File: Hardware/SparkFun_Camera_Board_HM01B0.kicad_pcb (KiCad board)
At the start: 4 copper layers, 22.9 x 35.6 mm, 114 parts, among them J1 Conn_01x09, J2 Conn_01x09, J3 Conn_01x09, J4 HM01B0, Q1 RE1C002UNTCL, Q2 RE1C002UNTCL, Q3 RE1C002UNTCL, Q4 RE1C002UNTCL, U1 HM01B0, U2 RT9080-2.8V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

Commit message: Rename MCLK to XCLK
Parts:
- removed kibuzzard-67D1FE09: G***, kibuzzard-67D1FE09
- added kibuzzard-681E5ABB: G***, kibuzzard-681E5ABB, F.Cu at (134.0, 112.1)
- JP4: value MCLK -> XCLK
- JP5: value OSC -> OSC_DIS
- JP6: value MCLK_GND -> XCLK_GND
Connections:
- net CAM_MCLK renamed CAM_XCLK
- net MCLK renamed XCLK

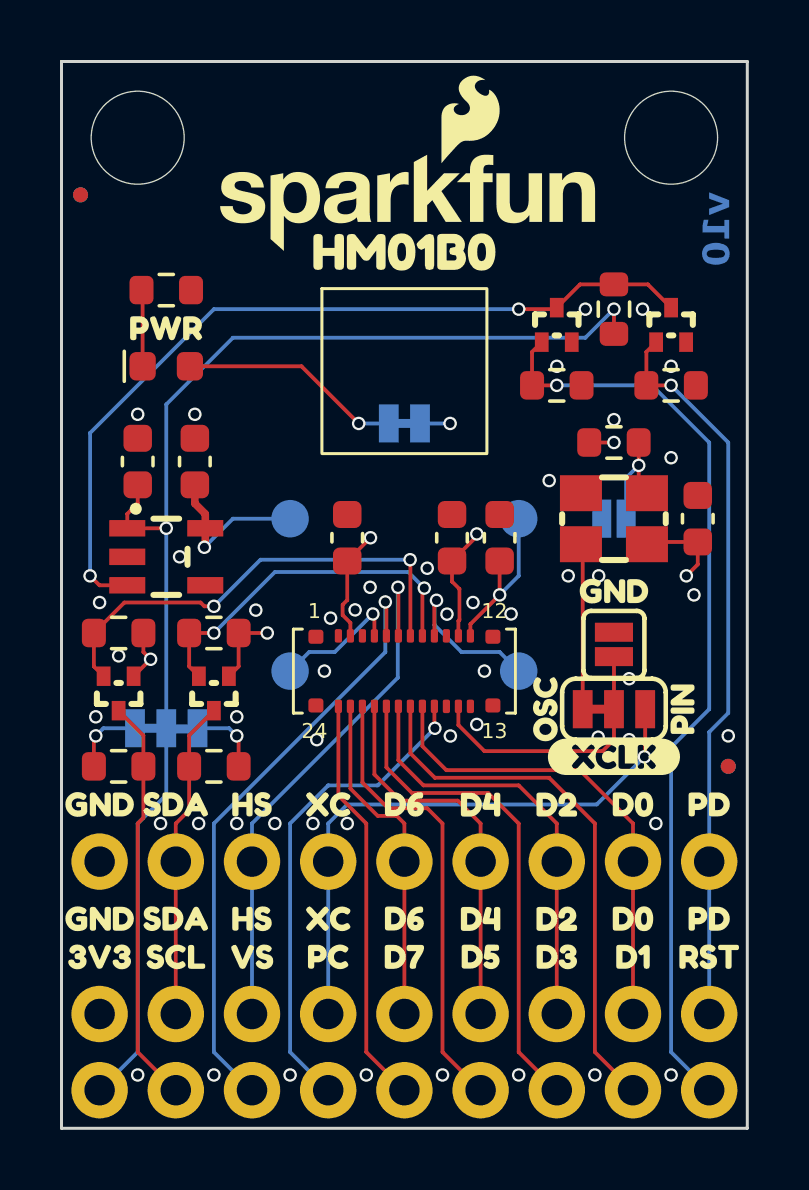
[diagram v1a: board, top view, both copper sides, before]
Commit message: Change XCLK jumpers to 3x 2-pad jumpers
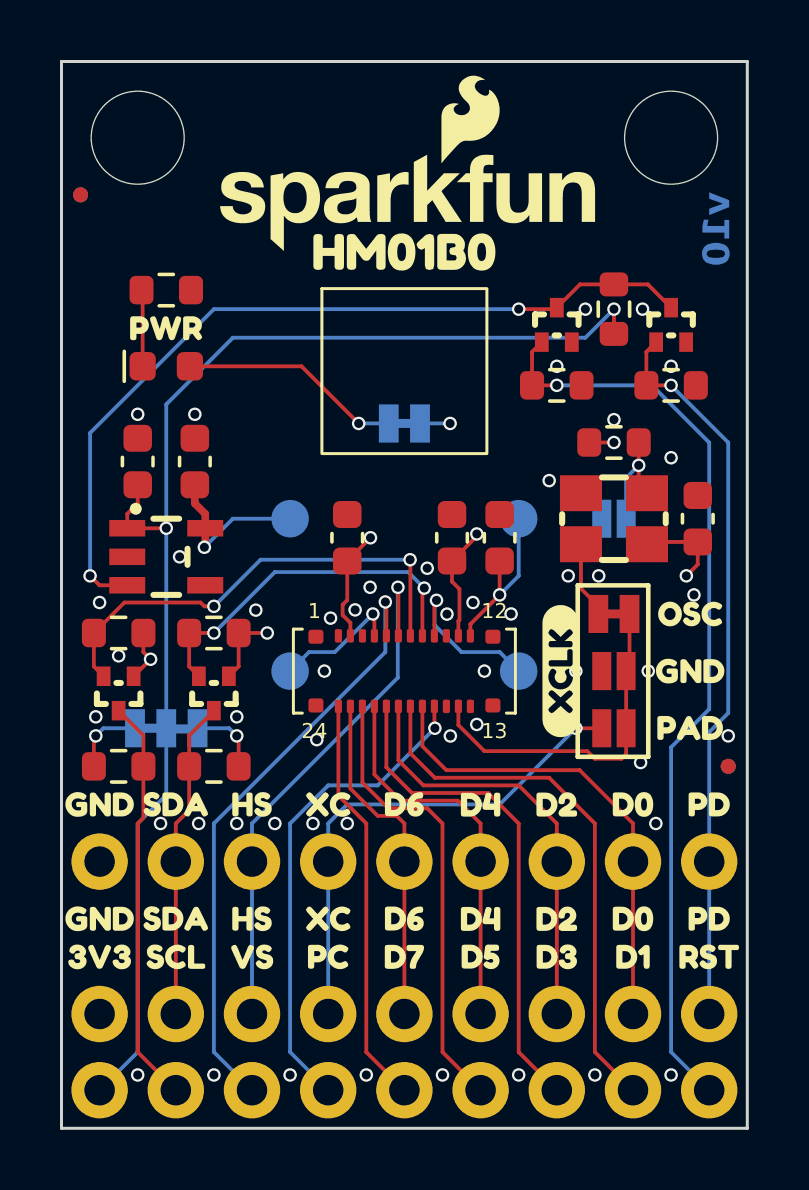
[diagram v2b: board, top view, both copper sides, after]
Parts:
- removed JP4: XCLK, SparkFun-Jumper:Jumper_3_NC-1_Trace
- removed kibuzzard-681E4657: G***, kibuzzard-681E4657
- removed kibuzzard-681E5ABB: G***, kibuzzard-681E5ABB
- added JP2: XCLK_PAD, SparkFun-Jumper:Jumper_2_NO_NoSilk, F.Cu at (134.0, 111.1)
- added JP3: XCLK_OSC, SparkFun-Jumper:Jumper_2_NC_Trace_NoSilk, F.Cu at (134.0, 107.3)
- added kibuzzard-681E60D5: G***, kibuzzard-681E60D5, F.Cu at (132.2, 109.2)
- added kibuzzard-681E611B: G***, kibuzzard-681E611B, F.Cu at (136.5, 111.1)
- JP6: footprint SparkFun-Jumper:Jumper_2_NO -> SparkFun-Jumper:Jumper_2_NO_NoSilk
- moved kibuzzard-681E464E 5.78 mm to (136.5, 107.3), turned to 0 degrees
- moved kibuzzard-681E465E 3.68 mm to (136.5, 109.2)
- moved JP6 0.89 mm to (134.0, 109.2), turned to 0 degrees
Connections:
- net XCLK renamed PAD_XCLK
- JP5 pad 2: Net-(JP5-B) -> Net-(JP3-A)
- R8 pad 1: Net-(JP5-B) -> Net-(JP3-A)
- Y1 pad 1: Net-(JP5-B) -> Net-(JP3-A)
- Y1 pad 3: Net-(JP4-A) -> Net-(JP3-A)
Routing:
- net Net-(JP3-A): track 0.00 -> 6.32 mm, vias 0 -> 1
- net Net-(JP4-A): track 5.52 -> 0.00 mm
- net Net-(JP5-B): track 3.76 -> 0.00 mm, vias 1 -> 0
- net PAD_XCLK: track 19.4 -> 16.8 mm
- net CAM_XCLK: track 9.10 -> 11.5 mm

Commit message: Fix incorrectly connected nets
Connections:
- JP5 pad 2: Net-(JP3-A) -> Net-(JP5-B)
- R8 pad 1: Net-(JP3-A) -> Net-(JP5-B)
- Y1 pad 1: Net-(JP3-A) -> Net-(JP5-B)
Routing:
- net Net-(JP5-B): track 0.00 -> 3.76 mm, vias 0 -> 1
- net Net-(JP3-A): track 6.32 -> 2.56 mm, vias 1 -> 0
